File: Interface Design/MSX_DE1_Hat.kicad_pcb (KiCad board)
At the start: 2 copper layers, 103 x 66 mm, 31 parts, among them J1 DE1 GPIO, J2 Conn_01x03_Male, J3 Conn_01x03_Male, J4 Conn_01x03_Male, J5 Conn_01x03_Male, J6 Conn_01x03_Male, J7 Conn_01x03_Male, U1 74LVC245A, U2 74LVC245A, U3 74LVC245A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

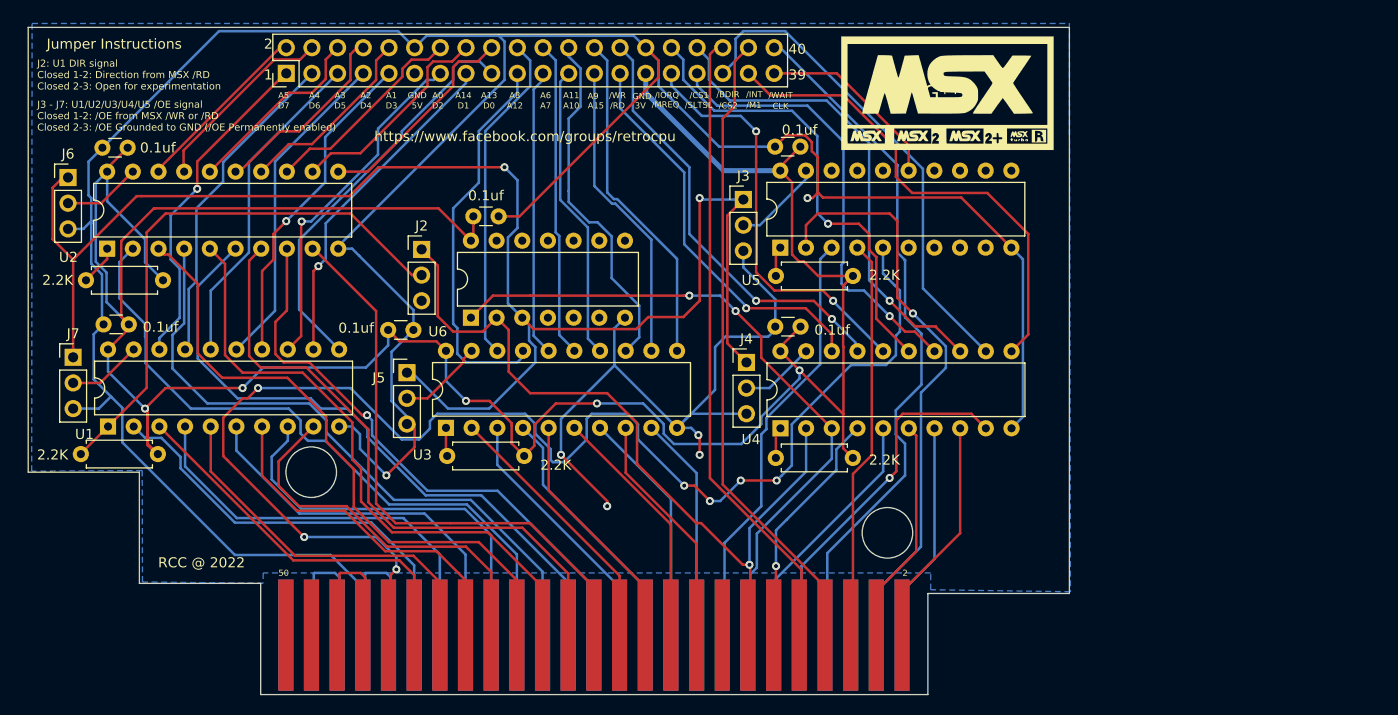
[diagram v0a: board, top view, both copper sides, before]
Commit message: Rev 1.1. Added pull ups for /OE; Changed Pull Ups to 10K; Changed silk screen
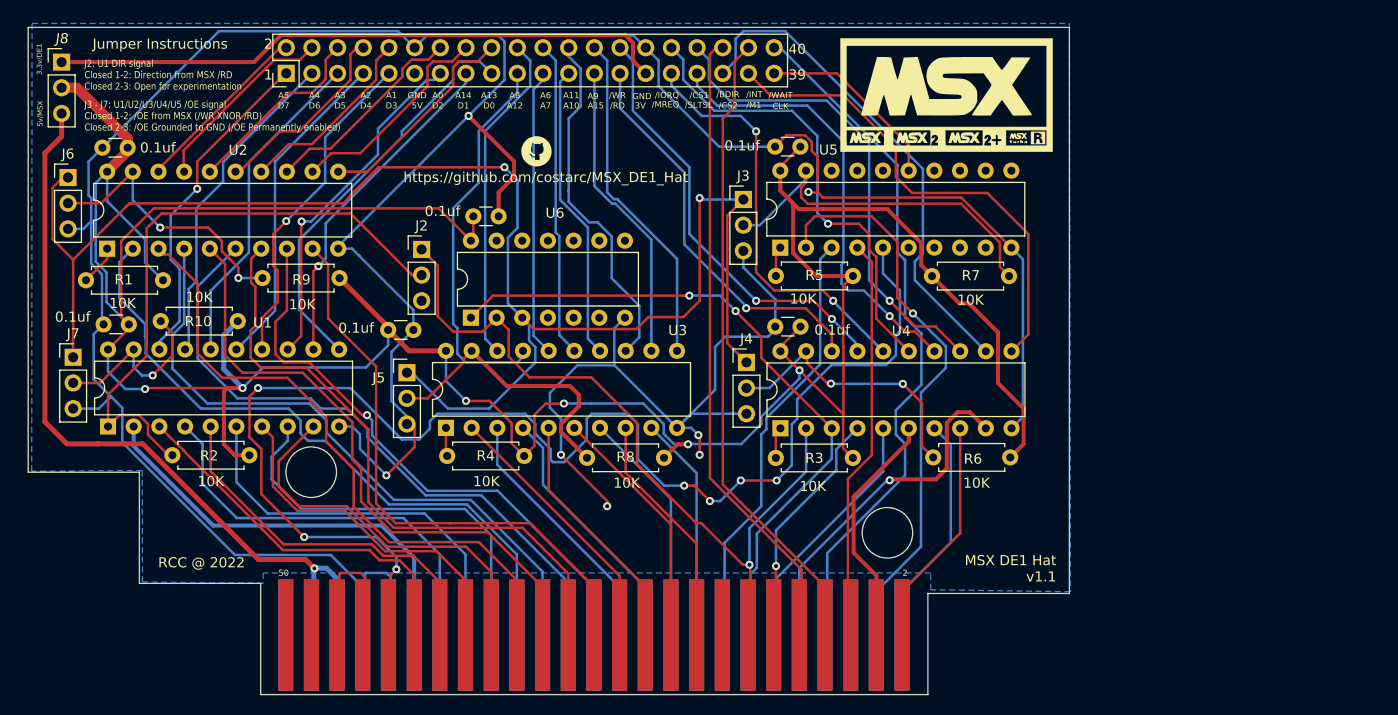
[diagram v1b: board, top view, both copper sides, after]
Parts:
- removed the G*** at (66.0, 32.0)
- removed the G*** at (107.2, 67.1)
- removed the G*** at (99.6, 51.8)
- removed the G*** at (110.7, 34.0)
- added G***: LOGO, LOGO, F.Cu at (102.2, 32.5)
- added J8: Conn_01x03_Male, Connector_PinHeader_2.54mm:PinHeader_1x03_P2.54mm_Vertical, F.Cu at (55.2, 23.6)
- added R10: 10K, Resistor_THT:R_Axial_DIN0207_L6.3mm_D2.5mm_P7.62mm_Horizontal, F.Cu at (72.7, 49.3)
- added R6: 10K, Resistor_THT:R_Axial_DIN0207_L6.3mm_D2.5mm_P7.62mm_Horizontal, F.Cu at (149.1, 62.7)
- added R7: 10K, Resistor_THT:R_Axial_DIN0207_L6.3mm_D2.5mm_P7.62mm_Horizontal, F.Cu at (141.3, 44.8)
- added R8: 10K, Resistor_THT:R_Axial_DIN0207_L6.3mm_D2.5mm_P7.62mm_Horizontal, F.Cu at (114.8, 62.8)
- added R9: 10K, Resistor_THT:R_Axial_DIN0207_L6.3mm_D2.5mm_P7.62mm_Horizontal, F.Cu at (82.7, 45.0)
- R1, R2, R3, R4, R5: value 2.2K -> 10K
- moved R2 9.06 mm to (73.8, 62.5)
- moved CD4077 / XNOR Truth Table 0.58 mm to (143.3, 26.8)
- moved G*** 0.20 mm to (142.8, 26.9)
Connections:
- C1 pad 2: +3.3V -> Vdd
- C2 pad 2: +3.3V -> Vdd
- C3 pad 2: +3.3V -> Vdd
- C4 pad 2: +3.3V -> Vdd
- C5 pad 2: +3.3V -> Vdd
- C6 pad 2: +3.3V -> Vdd
- R1 pad 1: +3.3V -> Vdd
- R2 pad 1: +3.3V -> Vdd
- R3 pad 1: +3.3V -> Vdd
- R4 pad 1: +3.3V -> Vdd
- R5 pad 1: +3.3V -> Vdd
- U1 pad 20: +3.3V -> Vdd
- U2 pad 20: +3.3V -> Vdd
- U3 pad 20: +3.3V -> Vdd
- U4 pad 20: +3.3V -> Vdd
- U5 pad 20: +3.3V -> Vdd
- U6 pad 14: +3.3V -> Vdd
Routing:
- net Vdd: track 0.00 -> 305.9 mm, vias 0 -> 6
- net +3.3V: track 256.4 -> 61.5 mm, vias 5 -> 0
- net +5V: track 14.9 -> 79.6 mm, vias 0 -> 1
- net Net-(J3-Pad2): track 9.04 -> 37.1 mm
- net Net-(J5-Pad2): track 8.54 -> 29.0 mm
- net Net-(J4-Pad2): track 7.41 -> 27.5 mm, vias 0 -> 2
- net Net-(J6-Pad2): track 7.70 -> 27.7 mm, vias 0 -> 2
- net Net-(J7-Pad2): track 7.62 -> 18.3 mm, vias 0 -> 1
- net GNDREF: track 377.0 -> 367.3 mm, vias 6 -> 7
- net Net-(J2-Pad2): track 55.1 -> 60.6 mm
- net D3: track 37.3 -> 39.1 mm
- net /CS12: track 57.9 -> 56.5 mm
- net /CS1: track 21.9 -> 23.2 mm
- net /SLTSL: track 22.5 -> 23.7 mm
- net D7: track 41.0 -> 41.9 mm
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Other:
- board text added: "3.3v/DE1"
- board text added: "5v/MSX"
- board text added: "J3 - J7: U1/U2/U3/U4/U5 /OE signal Closed 1-2: /OE from MSX (/WR XNOR /RD) Closed 2-3: /OE Grounded to GND (/OE Permanently enabled)"
- board text added: "MSX DE1 Hat v1.1"
- board text added: "https://github.com/costarc/MSX_DE1_Hat"
- board text removed: "J3 - J7: U1/U2/U3/U4/U5 /OE signal Closed 1-2: /OE from MSX /WR or /RD Closed 2-3: /OE Grounded to GND (/OE Permanently enabled)"
- board text removed: "https://www.facebook.com/groups/retrocpu"

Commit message: .
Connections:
- J1 pad 40: /WAIT -> /C_WAIT
- J2 pad 2: Net-(J2-Pad2) -> Net-(R5-Pad2)
- R1 pad 2: Net-(R1-Pad2) -> Net-(R5-Pad2)
- R2 pad 2: Net-(J2-Pad2) -> Net-(R5-Pad2)
- R3 pad 2: Net-(R3-Pad2) -> Net-(R5-Pad2)
- R4 pad 2: Net-(R4-Pad2) -> Net-(R5-Pad2)
- U1 pad 1: Net-(J2-Pad2) -> Net-(R5-Pad2)
- U2 pad 1: Net-(R1-Pad2) -> Net-(R5-Pad2)
- U3 pad 1: Net-(R4-Pad2) -> Net-(R5-Pad2)
- U4 pad 1: Net-(R3-Pad2) -> Net-(R5-Pad2)
- U5 pad 14: unconnected-(U5-Pad14) -> /C_WAIT
- U5 pad 6: unconnected-(U5-Pad6) -> /WAIT
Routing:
- net Net-(R5-Pad2): track 2.98 -> 188.2 mm, vias 0 -> 3
- net Net-(J2-Pad2): track 60.6 -> 0.00 mm
- net /WAIT: track 69.4 -> 44.0 mm
- net /C_WAIT: track 0.00 -> 21.3 mm
- net Net-(R1-Pad2): track 3.99 -> 0.00 mm
- net Net-(R3-Pad2): track 3.12 -> 0.00 mm
- net Net-(R4-Pad2): track 2.83 -> 0.00 mm
- net /C_MREQ: track 41.2 -> 40.1 mm
- net /INT: track 63.6 -> 64.3 mm
- net Net-(J3-Pad1): track 154.8 -> 155.5 mm
- net Net-(J5-Pad2): track 29.0 -> 29.6 mm
- net GNDREF: track 367.3 -> 366.7 mm

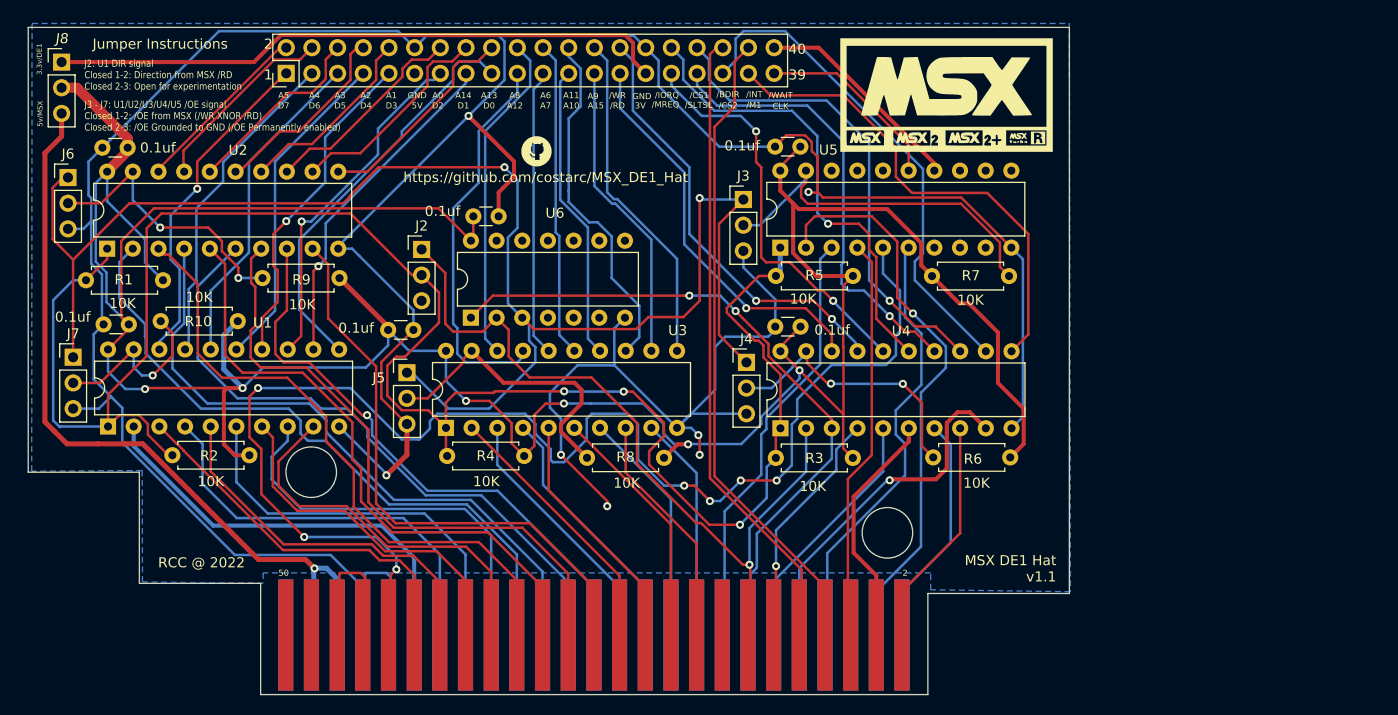
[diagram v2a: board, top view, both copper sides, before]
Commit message: Updated PCB Rev 1.1 with IDC connector in right position
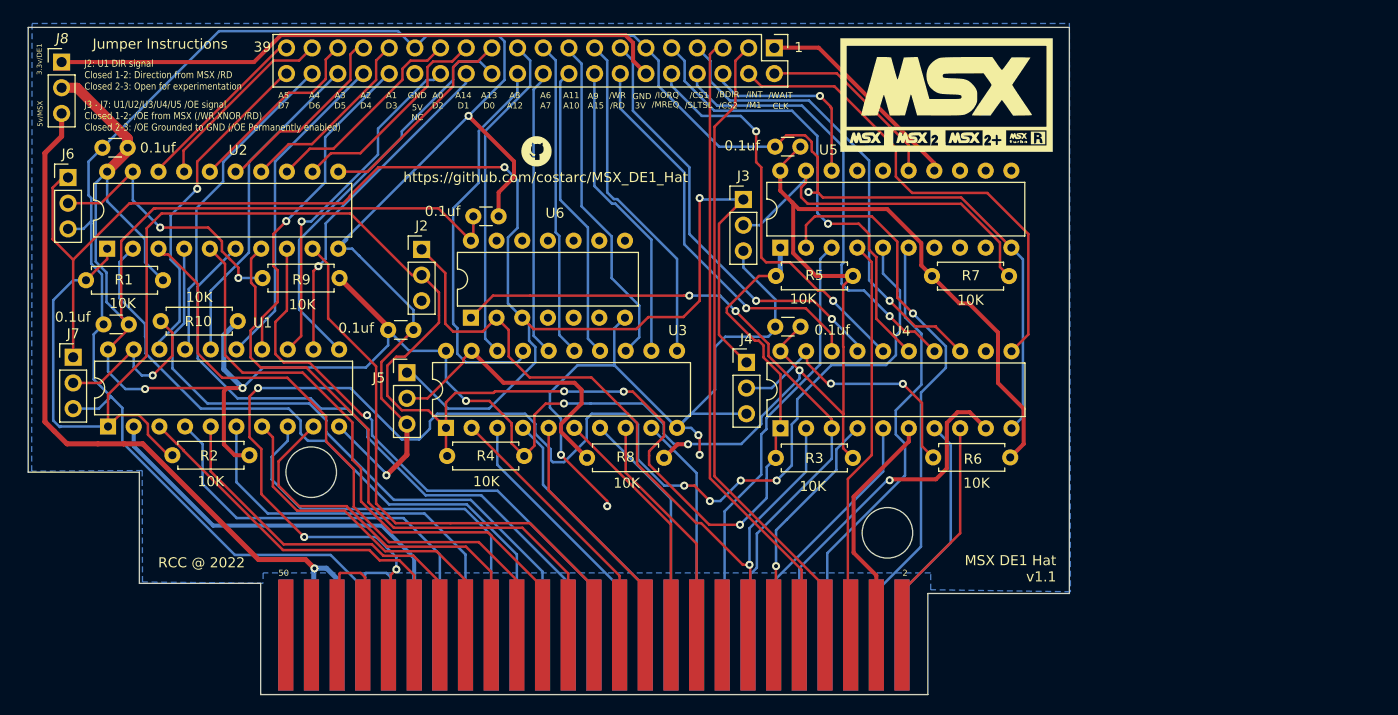
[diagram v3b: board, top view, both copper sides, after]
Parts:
- moved J1 48.3 mm to (125.8, 22.2), turned to -90 degrees
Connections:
- J1 pad 1: C_D7 -> /C_WAIT
- J1 pad 10: C_A1 -> /C_MREQ
- J1 pad 11: unconnected-(J1-Pad11) -> GNDREF
- J1 pad 12: GNDREF -> +3.3V
- J1 pad 13: C_D2 -> /C_WR
- J1 pad 14: C_A0 -> /C_RD
- J1 pad 15: C_D1 -> C_A9
- J1 pad 16: C_A14 -> C_A15
- J1 pad 17: C_D0 -> C_A11
- J1 pad 18: C_A13 -> C_A10
- J1 pad 19: C_A12 -> C_A6
- J1 pad 2: C_A5 -> C_CLOCK
- J1 pad 20: C_A8 -> C_A7
- J1 pad 21: C_A7 -> C_A8
- J1 pad 22: C_A6 -> C_A12
- J1 pad 23: C_A10 -> C_A13
- J1 pad 24: C_A11 -> C_D0
- J1 pad 25: C_A15 -> C_A14
- J1 pad 26: C_A9 -> C_D1
- J1 pad 27: /C_RD -> C_A0
- J1 pad 28: /C_WR -> C_D2
- J1 pad 29: +3.3V -> GNDREF
- J1 pad 3: C_D6 -> /INT
- J1 pad 30: GNDREF -> unconnected-(J1-Pad30)
- J1 pad 31: /C_MREQ -> C_A1
- J1 pad 32: /C_IORQ -> C_D3
- J1 pad 33: /C_SLTSL -> C_A2
- J1 pad 34: /C_CS1 -> C_D4
- J1 pad 35: /C_CS2 -> C_A3
- J1 pad 36: /BUSDIR -> C_D5
- J1 pad 37: /C_M1 -> C_A4
- J1 pad 38: /INT -> C_D6
- J1 pad 39: C_CLOCK -> C_A5
- J1 pad 4: C_A4 -> /C_M1
- J1 pad 40: /C_WAIT -> C_D7
- J1 pad 5: C_D5 -> /BUSDIR
- J1 pad 6: C_A3 -> /C_CS12
- J1 pad 7: C_D4 -> /C_CS1
- J1 pad 8: C_A2 -> /C_SLTSL
- J1 pad 9: C_D3 -> /C_IORQ
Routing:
- net /C_CS2: track 49.7 -> 0.00 mm
- net /C_CS12: track 0.00 -> 18.9 mm, vias 0 -> 1
- net GNDREF: track 366.7 -> 368.2 mm
- net C_A11: track 34.9 -> 33.4 mm
- net /C_CS1: track 47.6 -> 46.6 mm
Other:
- board text added: "5V NC"
- board text removed: "40"
- board text removed: "5V"

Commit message: Added working firmware / vhdl. Updated schematic and pcb to rmove not needed components
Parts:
- removed C6: 0.1uf, Capacitor_THT:C_Disc_D3.0mm_W1.6mm_P2.50mm
- removed J2, J3, J4, J6, J7: Conn_01x03_Male, Connector_PinHeader_2.54mm:PinHeader_1x03_P2.54mm_Vertical
- removed U6: 4077, Package_DIP:DIP-14_W7.62mm
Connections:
- R1 pad 2: Net-(J2-Pad2) -> Net-(R1-Pad2)
- R2 pad 2: Net-(J2-Pad2) -> /RD
- R3 pad 2: Net-(J2-Pad2) -> Net-(R3-Pad2)
- R4 pad 2: Net-(J2-Pad2) -> Net-(R4-Pad2)
- R5 pad 2: Net-(J2-Pad2) -> Net-(R5-Pad2)
- U1 pad 1: Net-(J2-Pad2) -> /RD
- U1 pad 19: Net-(J7-Pad2) -> unconnected-(U1-Pad19)
- U2 pad 1: Net-(J2-Pad2) -> Net-(R1-Pad2)
- U2 pad 19: Net-(J6-Pad2) -> GNDREF
- U3 pad 1: Net-(J2-Pad2) -> Net-(R4-Pad2)
- U3 pad 19: Net-(J5-Pad2) -> GNDREF
- U4 pad 1: Net-(J2-Pad2) -> Net-(R3-Pad2)
- U4 pad 19: Net-(J4-Pad2) -> GNDREF
- U5 pad 1: Net-(J2-Pad2) -> Net-(R5-Pad2)
- U5 pad 12: unconnected-(U5-Pad12) -> /BUSDIR
- U5 pad 13: unconnected-(U5-Pad13) -> /INT
- U5 pad 14: /C_WAIT -> /WAIT
- U5 pad 19: Net-(J3-Pad2) -> GNDREF
- U5 pad 6: /WAIT -> /C_WAIT
- U5 pad 7: unconnected-(U5-Pad7) -> /C_INT
- U5 pad 8: unconnected-(U5-Pad8) -> /C_BUSDIR
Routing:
- net Net-(J2-Pad2): track 188.2 -> 0.00 mm, vias 3 -> 0
- net Net-(R1-Pad2): track 0.00 -> 171.3 mm, vias 0 -> 3
- net Net-(J3-Pad1): track 155.5 -> 55.4 mm, vias 2 -> 1
- net Vdd: track 305.9 -> 258.6 mm
- net /WR: track 67.3 -> 24.0 mm, vias 2 -> 0
- net Net-(J6-Pad2): track 27.7 -> 0.01 mm, vias 2 -> 0
- net /WAIT: track 44.0 -> 21.3 mm
- net /C_WAIT: track 21.3 -> 44.0 mm
- net /RD: track 76.3 -> 54.8 mm
- net GNDREF: track 368.2 -> 351.6 mm
- net C_A12: track 38.2 -> 36.7 mm

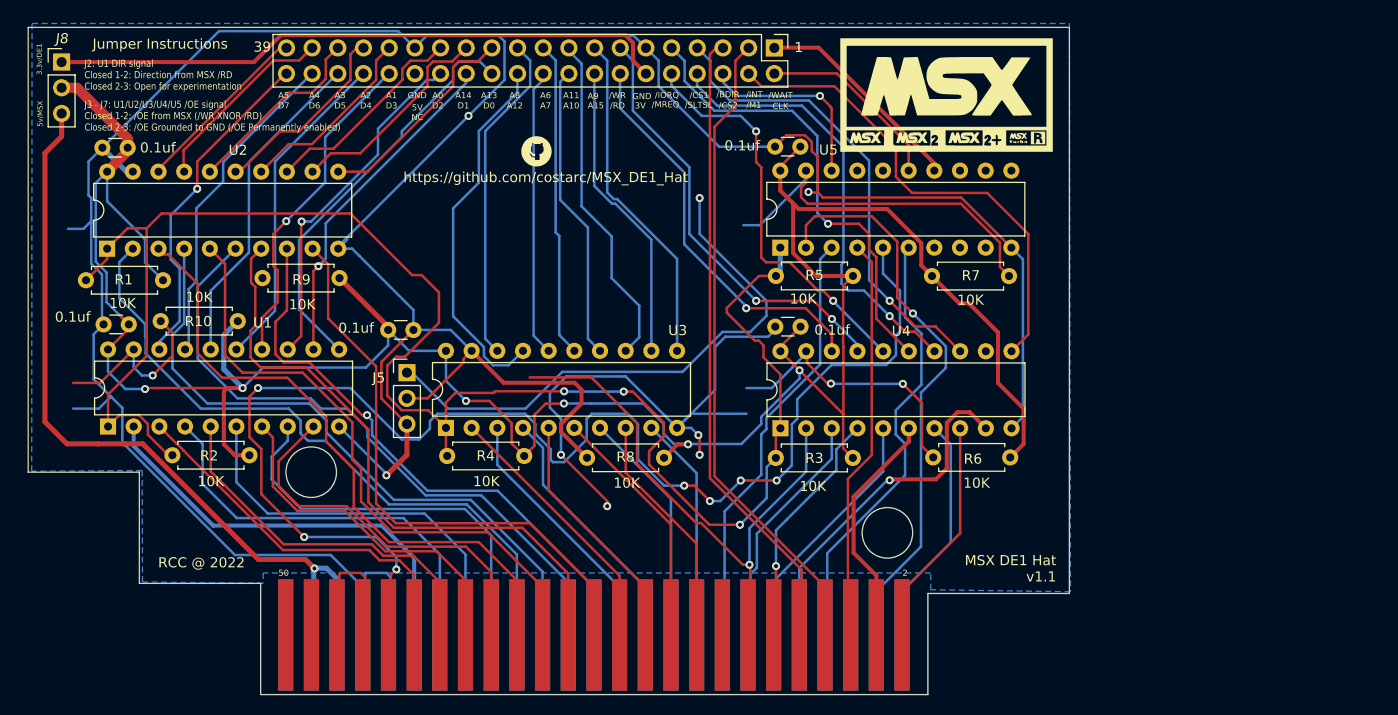
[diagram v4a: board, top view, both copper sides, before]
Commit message: Starting routing of reivsed pcb
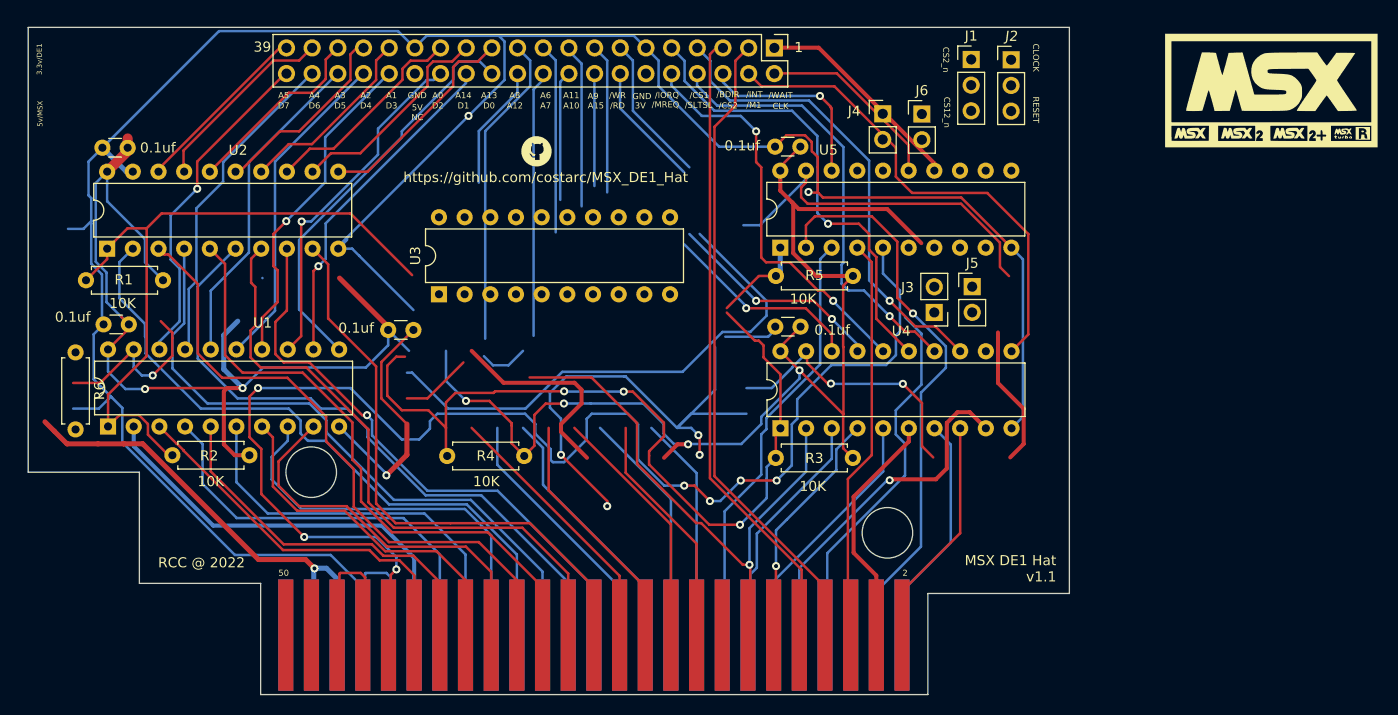
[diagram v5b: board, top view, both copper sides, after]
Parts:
- removed R10, R7, R8, R9: 10K, Resistor_THT:R_Axial_DIN0207_L6.3mm_D2.5mm_P7.62mm_Horizontal
- added J1: J1, Connector_PinHeader_2.54mm:PinHeader_1x03_P2.54mm_Vertical, F.Cu at (145.2, 23.4)
- added J3: J3, Connector_PinHeader_2.54mm:PinHeader_1x02_P2.54mm_Vertical, F.Cu at (141.6, 48.4)
- added J4: J4, Connector_PinHeader_2.54mm:PinHeader_1x02_P2.54mm_Vertical, F.Cu at (136.5, 28.8)
- added J6: J6, Connector_PinHeader_2.54mm:PinHeader_1x02_P2.54mm_Vertical, F.Cu at (140.3, 28.8)
- J2: renamed from J8; value Conn_01x03_Male -> J2
- J5: value Conn_01x03_Male -> J5; footprint Connector_PinHeader_2.54mm:PinHeader_1x03_P2.54mm_Vertical -> Connector_PinHeader_2.54mm:PinHeader_1x02_P2.54mm_Vertical
- moved J2 93.9 mm to (149.2, 23.4)
- moved R6 93.0 mm to (56.6, 52.4), turned to -90 degrees
- moved J5 56.6 mm to (145.3, 45.9)
- moved CD4077 / XNOR Truth Table 36.3 mm to (174.2, 7.87)
- moved G*** 32.1 mm to (174.9, 26.4)
- moved U3 13.2 mm to (92.6, 46.6)
- renumbered J1 to IDC1
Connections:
- IDC1 pad 11: GNDREF -> unconnected-(IDC1-Pad11)
- IDC1 pad 12: +3.3V -> GNDREF
- IDC1 pad 2: C_CLOCK -> C_CLK_OR_RST
- IDC1 pad 29: GNDREF -> Vdd
- IDC1 pad 3: /INT -> /C_INT
- IDC1 pad 30: unconnected-(J1-Pad30) -> GNDREF
- IDC1 pad 5: /BUSDIR -> /C_BUSDIR
- IDC1 pad 6: /C_CS12 -> C_CS2_CS12
- J2 pad 1: +3.3V -> C_CLOCK
- J2 pad 2: Vdd -> C_CLK_OR_RST
- J2 pad 3: +5V -> /C_RESET
- J5 pad 1: Net-(J3-Pad1) -> unconnected-(J5-Pad1)
- R6 pad 2: Net-(J4-Pad2) -> /C_BUSDIR
- U1 pad 19: unconnected-(U1-Pad19) -> /C_BUSDIR
- U5 pad 11: unconnected-(U5-Pad11) -> /WAIT
- U5 pad 12: /BUSDIR -> /INT
- U5 pad 13: /INT -> /BUSDIR
- U5 pad 14: /WAIT -> Net-(J6-Pad1)
- U5 pad 16: /C_RFSH -> Net-(J4-Pad1)
- U5 pad 4: /RFSH -> Net-(J3-Pad2)
- U5 pad 6: /C_WAIT -> Net-(J5-Pad2)
- U5 pad 7: /C_INT -> /C_BUSDIR
- U5 pad 8: /C_BUSDIR -> /C_INT
- U5 pad 9: unconnected-(U5-Pad9) -> /C_WAIT
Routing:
- net Net-(R1-Pad2): track 171.3 -> 68.4 mm, vias 3 -> 0
- net Net-(R3-Pad2): track 0.00 -> 82.1 mm, vias 0 -> 3
- net +3.3V: track 61.5 -> 0.00 mm
- net Net-(J3-Pad1): track 55.4 -> 0.00 mm, vias 1 -> 0
- net GNDREF: track 351.6 -> 405.7 mm, vias 7 -> 9
- net (no net): track 0.00 -> 51.7 mm
- net /C_WAIT: track 44.0 -> 0.00 mm
- net /RFSH: track 40.3 -> 0.00 mm
- net Vdd: track 258.6 -> 219.9 mm
- net +5V: track 79.6 -> 48.4 mm
- net Net-(J4-Pad2): track 27.6 -> 0.00 mm, vias 2 -> 0
- net Net-(J6-Pad1): track 0.00 -> 21.3 mm
- net C_A12: track 36.7 -> 17.2 mm
- net /C_CS12: track 18.9 -> 0.00 mm, vias 1 -> 0
- net C_CS2_CS12: track 0.00 -> 18.9 mm, vias 0 -> 1
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- removed copper zone on B.Cu, net GNDREF
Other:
- board text added: "CLOCK"
- board text added: "CS12_n"
- board text added: "CS2_n"
- board text added: "RESET"
- board text removed: "J2: U1 DIR signal Closed 1-2: Direction from MSX /RD Closed 2-3: Open for experimentation"
- board text removed: "J3 - J7: U1/U2/U3/U4/U5 /OE signal Closed 1-2: /OE from MSX (/WR XNOR /RD) Closed 2-3: /OE Grounded to GND (/OE Permanently enabled)"
- board text removed: "Jumper Instructions"
